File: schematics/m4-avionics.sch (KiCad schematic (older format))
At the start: 3 parts

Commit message: Rename schematics folder and delete old board template
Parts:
- added J?: CAMERA, symbol cusf-kicad:CONN_02x12
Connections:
- net 3v3: now also J?.1, J?.2, J?.3, J?.4
- net GND: now also J?.21, J?.22, J?.23, J?.24
- new net DCMI_D0: J?.5
- new net DCMI_D1: J?.6
- new net DCMI_D2: J?.7
- new net DCMI_D3: J?.8
- new net DCMI_D4: J?.9
- new net DCMI_D5: J?.10
- new net DCMI_D6: J?.11
- new net DCMI_D7: J?.12
- new net DCMI_HSYNC: J?.13
- new net DCMI_NRST: J?.16
- new net DCMI_PIXCLK: J?.17
- new net DCMI_PWR_EN: J?.14
- new net DCMI_SCL: J?.20
- new net DCMI_SDA: J?.18
- new net DCMI_VSYNC: J?.15
- no-connect marks 0 -> 1
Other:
- note added: "CAMERA INTERCONNECT"
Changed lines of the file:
@@
 Text Label 1300 5650 0    50   ~ 0
 CAN_BUS
+$Comp
+L cusf-kicad:CONN_02x12 J?
+U 1 1 621A1F39
+P 9900 3900
+F 0 "J?" H 9850 4000 50  0000 C CNN
+F 1 "CAMERA" H 9850 2700 50  0000 C CNN
+F 2 "" H 9900 3900 50  0001 C CNN
+F 3 "" H 9900 3900 50  0001 C CNN
+	1    9900 3900
+	1    0    0    -1
+$EndComp
+Wire Wire Line
+	9700 4000 9600 4000
+Wire Wire Line
+	9600 4000 9600 3900
+Wire Wire Line
+	9600 3900 9700 3900
+Wire Wire Line
+	10000 3900 10100 3900
+Wire Wire Line
+	10100 3900 10100 4000
+Wire Wire Line
+	10000 4000 10100 4000
+Wire Wire Line
+	10100 3900 10100 3750
+Connection ~ 10100 3900
+Wire Wire Line
+	9600 3750 9600 3900
+Connection ~ 9600 3900
+$Comp
+L cusf-kicad:3v3 #PWR?
+U 1 1 621A1F49
+P 9600 3750
+F 0 "#PWR?" H 9600 3860 50  0001 L CNN
+F 1 "3v3" H 9600 3850 50  0000 C CNN
+F 2 "" H 9600 3750 50  0001 C CNN
+F 3 "" H 9600 3750 50  0001 C CNN
+	1    9600 3750
+	1    0    0    -1
+$EndComp
+$Comp
+L cusf-kicad:3v3 #PWR?
+U 1 1 621A1F4F
+P 10100 3750
+F 0 "#PWR?" H 10100 3860 50  0001 L CNN
+F 1 "3v3" H 10100 3850 50  0000 C CNN
+F 2 "" H 10100 3750 50  0001 C CNN
+F 3 "" H 10100 3750 50  0001 C CNN
+	1    10100 3750
+	1    0    0    -1
+$EndComp
+Wire Wire Line
+	9700 5000 9600 5000
+Wire Wire Line
+	9600 5000 9600 5150
+Wire Wire Line
+	9600 5000 9600 4900
+Wire Wire Line
+	9600 4900 9700 4900
+Connection ~ 9600 5000
+Wire Wire Line
+	10000 5000 10100 5000
+Wire Wire Line
+	10100 5000 10100 5150
+Wire Wire Line
+	10100 5000 10100 4900
+Wire Wire Line
+	10100 4900 10000 4900
+Connection ~ 10100 5000
+$Comp
+L cusf-kicad:GND #PWR?
+U 1 1 621A1F5F
+P 9600 5150
+F 0 "#PWR?" H 9470 5190 50  0001 L CNN
+F 1 "GND" H 9600 5050 50  0000 C CNN
+F 2 "" H 9600 5150 50  0001 C CNN
+F 3 "" H 9600 5150 50  0001 C CNN
+	1    9600 5150
+	1    0    0    -1
+$EndComp
+$Comp
+L cusf-kicad:GND #PWR?
+U 1 1 621A1F65
+P 10100 5150
+F 0 "#PWR?" H 9970 5190 50  0001 L CNN
+F 1 "GND" H 10100 5050 50  0000 C CNN
+F 2 "" H 10100 5150 50  0001 C CNN
+F 3 "" H 10100 5150 50  0001 C CNN
+	1    10100 5150
+	1    0    0    -1
+$EndComp
+Wire Wire Line
+	9700 4100 9600 4100
+Wire Wire Line
+	9700 4200 9600 4200
+Wire Wire Line
+	9700 4300 9600 4300
+Wire Wire Line
+	9700 4400 9600 4400
+Wire Wire Line
+	9700 4500 9600 4500
+Wire Wire Line
+	10000 4100 10100 4100
+Wire Wire Line
+	10000 4200 10100 4200
+Wire Wire Line
+	10000 4300 10100 4300
+Wire Wire Line
+	10000 4400 10100 4400
+Wire Wire Line
+	10000 4500 10100 4500
+Wire Wire Line
+	10100 4600 10000 4600
+Wire Wire Line
+	10100 4700 10000 4700
+Wire Wire Line
+	9600 4700 9700 4700
+Wire Wire Line
+	9600 4600 9700 4600
+Text Label 10100 4100 0    50   ~ 0
+DCMI_D1
+Text Label 10100 4200 0    50   ~ 0
+DCMI_D3
+Text Label 10100 4300 0    50   ~ 0
+DCMI_D5
+Text Label 10100 4400 0    50   ~ 0
+DCMI_D7
+Text Label 9600 4400 2    50   ~ 0
+DCMI_D6
+Text Label 9600 4300 2    50   ~ 0
+DCMI_D4
+Text Label 9600 4200 2    50   ~ 0
+DCMI_D2
+Text Label 9600 4100 2    50   ~ 0
+DCMI_D0
+Text Label 9600 4700 2    50   ~ 0
+DCMI_PIXCLK
+Text Label 9600 4600 2    50   ~ 0
+DCMI_VSYNC
+Text Label 9600 4500 2    50   ~ 0
+DCMI_HSYNC
+Text Label 10100 4500 0    50   ~ 0
+DCMI_PWR_EN
+Text Label 10100 4600 0    50   ~ 0
+DCMI_NRST
+Wire Notes Line
+	8950 3400 10800 3400
+Wire Notes Line
+	10800 3400 10800 5550
+Wire Notes Line
+	10800 5550 8950 5550
+Wire Notes Line
+	8950 3400 8950 5550
+Text Notes 8950 3350 0    98   ~ 20
+CAMERA INTERCONNECT
+Wire Wire Line
+	10000 4800 10100 4800
+Text Label 10100 4700 0    50   ~ 0
+DCMI_SDA
+Text Label 10100 4800 0    50   ~ 0
+DCMI_SCL
+NoConn ~ 9700 4800
+Wire Wire Line
+	2650 1200 2800 1200
+Wire Wire Line
+	2650 2250 2800 2250
+Wire Wire Line
+	2650 3400 2800 3400
+$Comp
+L cusf-kicad:GND #PWR?
+U 1 1 621AB80D
+P 2800 3400
+F 0 "#PWR?" H 2670 3440 50  0001 L CNN
+F 1 "GND" V 2800 3150 50  0000 L CNN
+F 2 "" H 2800 3400 50  0001 C CNN
+F 3 "" H 2800 3400 50  0001 C CNN
+	1    2800 3400
+	0    -1   -1   0
+$EndComp
+$Comp
+L cusf-kicad:GND #PWR?
+U 1 1 621B0D14
+P 2800 2250
+F 0 "#PWR?" H 2670 2290 50  0001 L CNN
+F 1 "GND" V 2800 2000 50  0000 L CNN
+F 2 "" H 2800 2250 50  0001 C CNN
+F 3 "" H 2800 2250 50  0001 C CNN
+	1    2800 2250
+	0    -1   -1   0
+$EndComp
+$Comp
+L cusf-kicad:GND #PWR?
+U 1 1 621B11B9
+P 2800 1200
+F 0 "#PWR?" H 2670 1240 50  0001 L CNN
+F 1 "GND" V 2800 950 50  0000 L CNN
+F 2 "" H 2800 1200 50  0001 C CNN
+F 3 "" H 2800 1200 50  0001 C CNN
+	1    2800 1200
+	0    -1   -1   0
+$EndComp
 Wire Bus Line
 	1200 3800 1200 5500

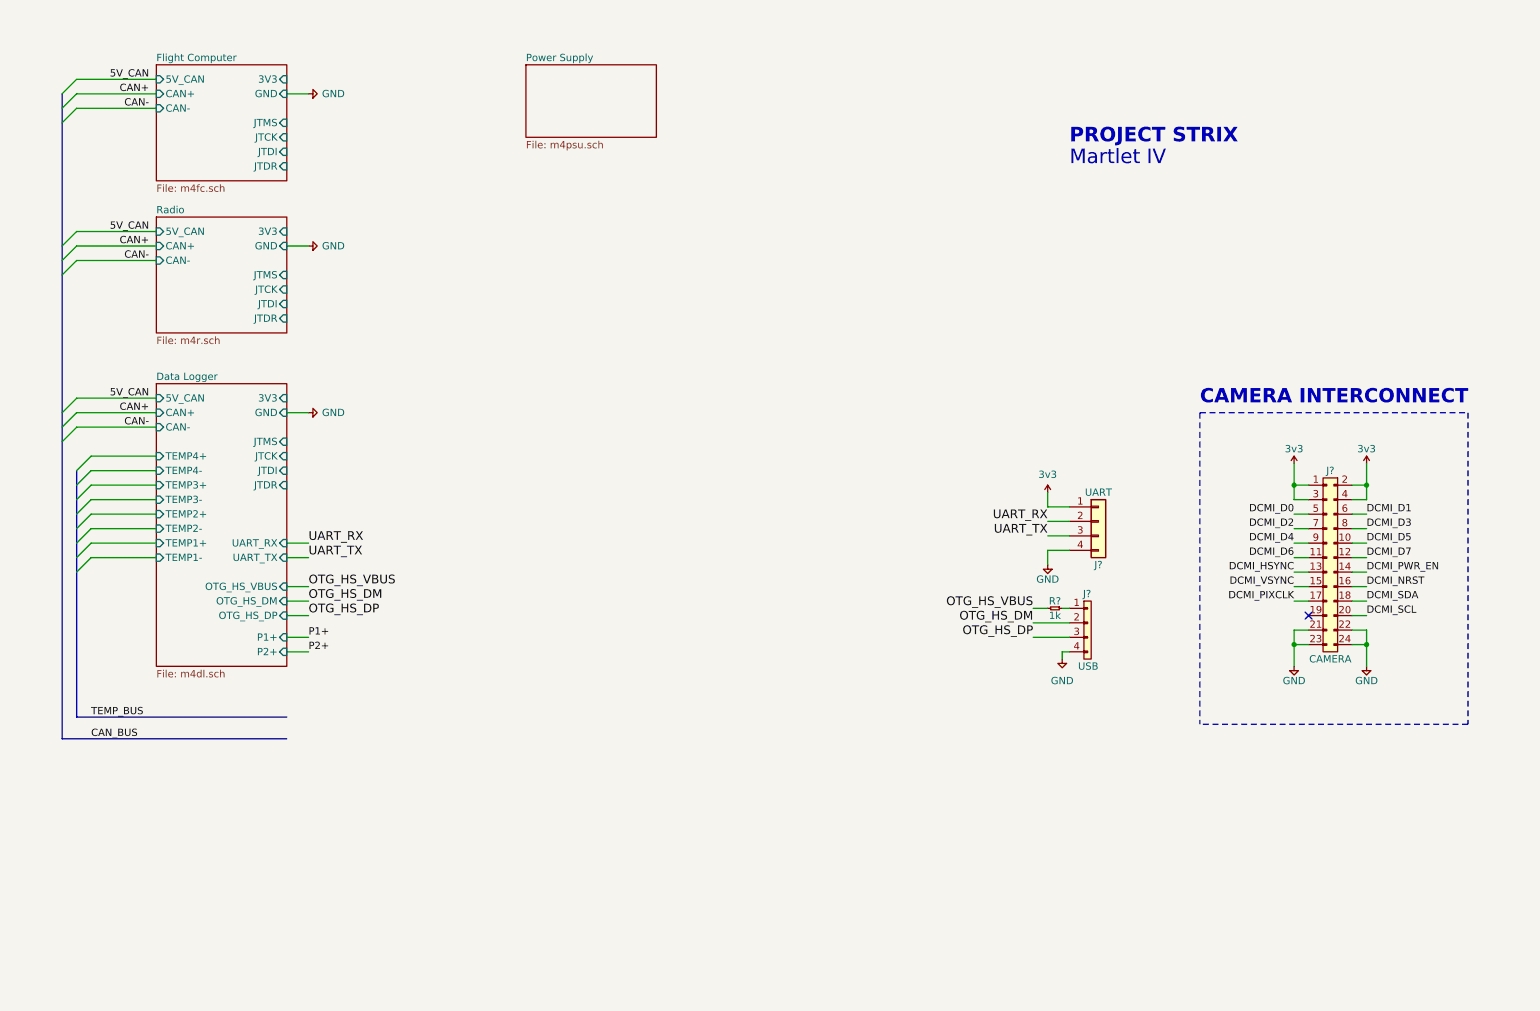
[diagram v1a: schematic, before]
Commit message: Chain JTAG connections
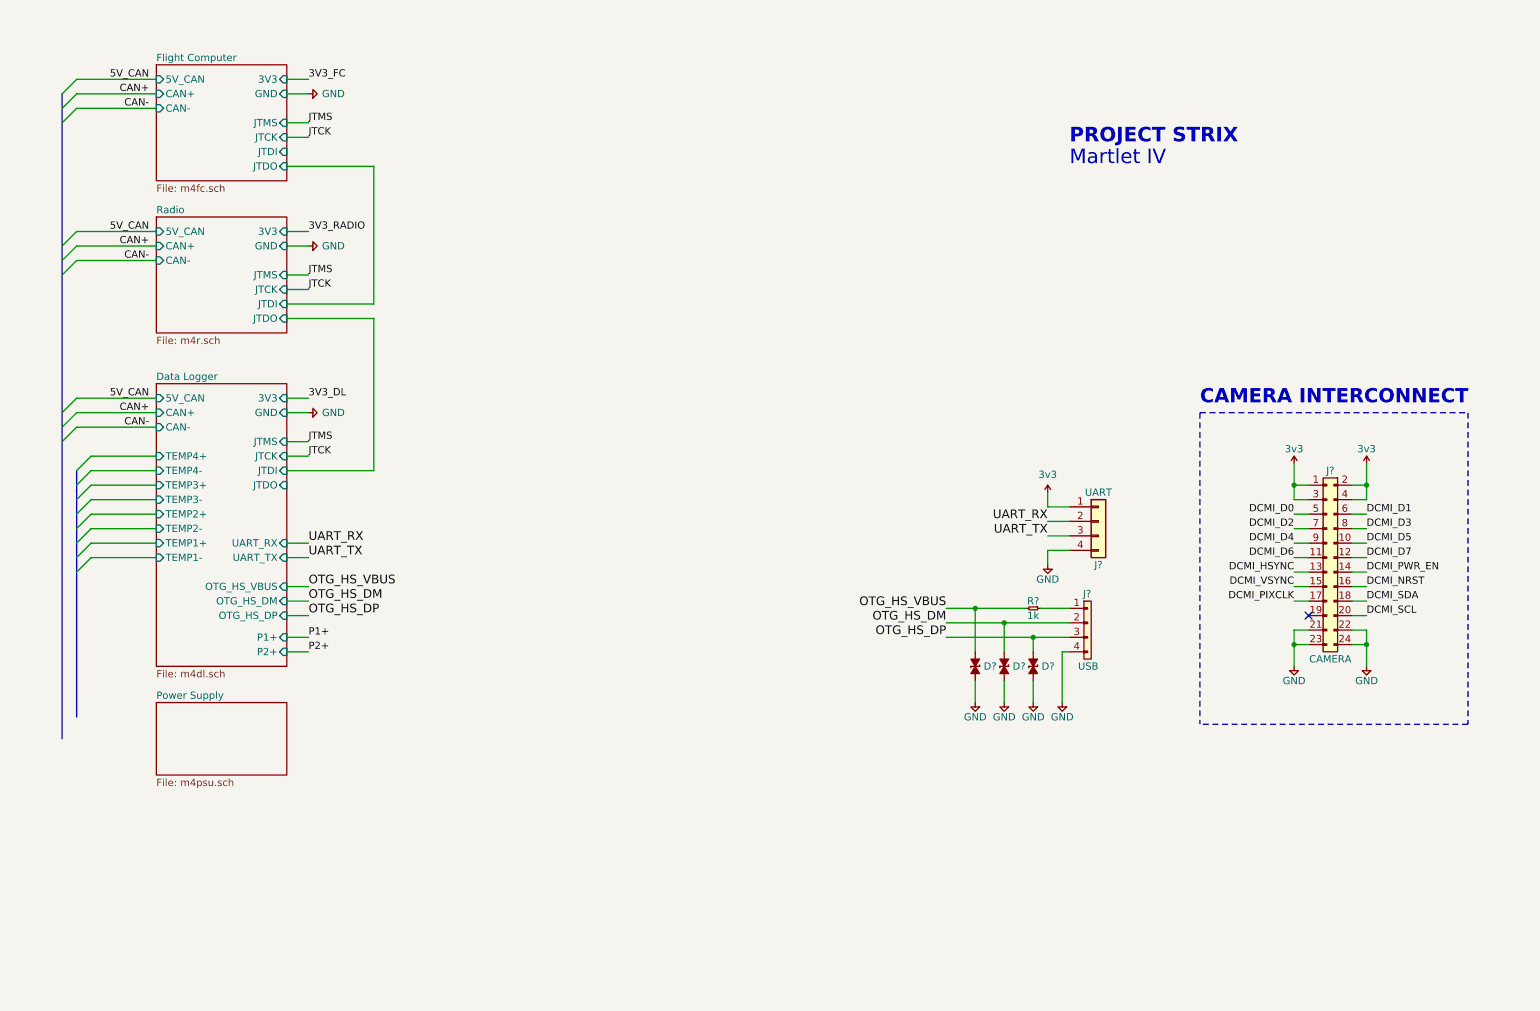
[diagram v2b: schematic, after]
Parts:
- added D? (x3): ESD_DIODE, cusf:0402, symbol cusf-kicad:ESD_DIODE
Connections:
- net GND: now also D?.2, D?.2, D?.2
- net OTG_HS_DM: now also D?.1
- net OTG_HS_DP: now also D?.1
- net OTG_HS_VBUS: now also D?.1
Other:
- moved on the sheet: R?
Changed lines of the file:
@@
 F8 "JTCK" I R 2650 3700 50
 F9 "JTDI" I R 2650 3800 50
-F10 "JTDR" I R 2650 3900 50
-F11 "TEMP4+" I L 1750 3700 50
-F12 "TEMP4-" I L 1750 3800 50
-F13 "TEMP3+" I L 1750 3900 50
-F14 "TEMP3-" I L 1750 4000 50
-F15 "TEMP2+" I L 1750 4100 50
-F16 "TEMP2-" I L 1750 4200 50
-F17 "TEMP1+" I L 1750 4300 50
-F18 "TEMP1-" I L 1750 4400 50
-F19 "3V3" I R 2650 3300 50
-F20 "GND" I R 2650 3400 50
-F21 "OTG_HS_VBUS" I R 2650 4600 50
-F22 "OTG_HS_DM" I R 2650 4700 50
-F23 "OTG_HS_DP" I R 2650 4800 50
-F24 "P1+" I R 2650 4950 50
-F25 "P2+" I R 2650 5050 50
+F10 "TEMP4+" I L 1750 3700 50
+F11 "TEMP4-" I L 1750 3800 50
+F12 "TEMP3+" I L 1750 3900 50
+F13 "TEMP3-" I L 1750 4000 50
+F14 "TEMP2+" I L 1750 4100 50
+F15 "TEMP2-" I L 1750 4200 50
+F16 "TEMP1+" I L 1750 4300 50
+F17 "TEMP1-" I L 1750 4400 50
+F18 "3V3" I R 2650 3300 50
+F19 "GND" I R 2650 3400 50
+F20 "OTG_HS_VBUS" I R 2650 4600 50
+F21 "OTG_HS_DM" I R 2650 4700 50
+F22 "OTG_HS_DP" I R 2650 4800 50
+F23 "P1+" I R 2650 4950 50
+F24 "P2+" I R 2650 5050 50
+F25 "JTDO" I R 2650 3900 50
 $EndSheet
 $Sheet
-S 4300 1000 900  500
+S 1750 5400 900  500
 U 6013B1F2
 F0 "Power Supply" 50
@@
 CAN-
 $Sheet
-S 1750 1000 900  800
-U 6013AEF4
-F0 "Flight Computer" 50
-F1 "m4fc.sch" 50
-F2 "5V_CAN" I L 1750 1100 50
-F3 "CAN+" I L 1750 1200 50
-F4 "CAN-" I L 1750 1300 50
-F5 "JTMS" I R 2650 1400 50
-F6 "JTCK" I R 2650 1500 50
-F7 "JTDI" I R 2650 1600 50
-F8 "JTDR" I R 2650 1700 50
-F9 "3V3" I R 2650 1100 50
-F10 "GND" I R 2650 1200 50
-$EndSheet
-$Sheet
 S 1750 2050 900  800
 U 6013B1C8
@@
 F6 "JTCK" I R 2650 2550 50
 F7 "JTDI" I R 2650 2650 50
-F8 "JTDR" I R 2650 2750 50
-F9 "3V3" I R 2650 2150 50
-F10 "GND" I R 2650 2250 50
+F8 "3V3" I R 2650 2150 50
+F9 "GND" I R 2650 2250 50
+F10 "JTDO" I R 2650 2750 50
 $EndSheet
 $Bitmap
@@
 L cusf-kicad:R R?
 U 1 1 61A0226B
-P 8000 4750
+P 7850 4750
 AR Path="/6013AE2F/61A0226B" Ref="R?"  Part="1"
 AR Path="/61A0226B" Ref="R?"  Part="1"
-F 0 "R?" H 8050 4800 50  0000 C CNN
-F 1 "1k" H 8050 4700 50  0000 C CNN
-F 2 "" H 8000 4750 50  0001 C CNN
-F 3 "" H 8000 4750 50  0001 C CNN
-	1    8000 4750
+F 0 "R?" H 7900 4800 50  0000 C CNN
+F 1 "1k" H 7900 4700 50  0000 C CNN
+F 2 "" H 7850 4750 50  0001 C CNN
+F 3 "" H 7850 4750 50  0001 C CNN
+	1    7850 4750
 	-1   0    0    -1
 $EndComp
@@
 L cusf-kicad:GND #PWR?
 U 1 1 61A02271
-P 8000 5100
+P 8000 5400
 AR Path="/6013AE2F/61A02271" Ref="#PWR?"  Part="1"
 AR Path="/61A02271" Ref="#PWR?"  Part="1"
-F 0 "#PWR?" H 8000 4850 50  0001 C CNN
-F 1 "GND" H 8000 4950 50  0000 C CNN
-F 2 "" H 8000 5100 50  0000 C CNN
-F 3 "" H 8000 5100 50  0000 C CNN
-	1    8000 5100
+F 0 "#PWR?" H 8000 5150 50  0001 C CNN
+F 1 "GND" H 8000 5300 50  0000 C CNN
+F 2 "" H 8000 5400 50  0000 C CNN
+F 3 "" H 8000 5400 50  0000 C CNN
+	1    8000 5400
 	-1   0    0    -1
 $EndComp
-Text Label 7800 4750 2    60   ~ 0
+Text Label 7200 4750 2    60   ~ 0
 OTG_HS_VBUS
-Text Label 7800 4850 2    60   ~ 0
+Text Label 7200 4850 2    60   ~ 0
 OTG_HS_DM
-Text Label 7800 4950 2    60   ~ 0
+Text Label 7200 4950 2    60   ~ 0
 OTG_HS_DP
 $Comp
@@
 $EndComp
 Wire Wire Line
-	8000 5050 8000 5100
-Wire Wire Line
-	8050 4750 8000 4750
+	8000 5050 8000 5400
+Wire Wire Line
+	8050 4750 7850 4750
 Wire Wire Line
 	8050 5050 8000 5050
@@
 	8050 4950 7800 4950
 Wire Wire Line
-	7800 4850 8050 4850
-Wire Wire Line
-	7900 4750 7800 4750
+	7200 4850 7600 4850
+Wire Wire Line
+	7750 4750 7400 4750
 Wire Wire Line
 	8050 4250 7900 4250
@@
 Wire Wire Line
 	2800 4400 2650 4400
-Wire Bus Line
-	1200 5500 2650 5500
 Entry Wire Line
 	1300 4300 1200 4400
@@
 Entry Wire Line
 	1200 1300 1100 1400
-Wire Bus Line
-	1100 5650 2650 5650
-Text Label 1300 5500 0    50   ~ 0
-TEMP_BUS
-Text Label 1300 5650 0    50   ~ 0
-CAN_BUS
 $Comp
 L cusf-kicad:CONN_02x12 J?
@@
 	0    -1   -1   0
 $EndComp
+$Sheet
+S 1750 1000 900  800
+U 6013AEF4
+F0 "Flight Computer" 50
+F1 "m4fc.sch" 50
+F2 "5V_CAN" I L 1750 1100 50
+F3 "CAN+" I L 1750 1200 50
+F4 "CAN-" I L 1750 1300 50
+F5 "JTMS" I R 2650 1400 50
+F6 "JTCK" I R 2650 1500 50
+F7 "JTDI" I R 2650 1600 50
+F8 "3V3" I R 2650 1100 50
+F9 "GND" I R 2650 1200 50
+F10 "JTDO" I R 2650 1700 50
+$EndSheet
+Wire Wire Line
+	2650 1700 3250 1700
+Wire Wire Line
+	3250 1700 3250 2650
+Wire Wire Line
+	3250 2650 2650 2650
+Wire Wire Line
+	2650 2750 3250 2750
+Wire Wire Line
+	3250 2750 3250 3800
+Wire Wire Line
+	3250 3800 2650 3800
+Wire Wire Line
+	2650 1500 2800 1500
+Wire Wire Line
+	2650 1400 2800 1400
+Text Label 2800 1400 0    50   ~ 0
+JTMS
+Text Label 2800 1500 0    50   ~ 0
+JTCK
+Wire Wire Line
+	2650 2550 2800 2550
+Wire Wire Line
+	2650 2450 2800 2450
+Text Label 2800 2450 0    50   ~ 0
+JTMS
+Text Label 2800 2550 0    50   ~ 0
+JTCK
+Wire Wire Line
+	2650 3700 2800 3700
+Wire Wire Line
+	2650 3600 2800 3600
+Text Label 2800 3600 0    50   ~ 0
+JTMS
+Text Label 2800 3700 0    50   ~ 0
+JTCK
+Wire Wire Line
+	2650 3300 2800 3300
+Text Label 2800 3300 0    50   ~ 0
+3V3_DL
+Wire Wire Line
+	2650 2150 2800 2150
+Text Label 2800 2150 0    50   ~ 0
+3V3_RADIO
+Wire Wire Line
+	2650 1100 2800 1100
+Text Label 2800 1100 0    50   ~ 0
+3V3_FC
+$Comp
+L cusf-kicad:ESD_DIODE D?
+U 1 1 601F8D2D
+P 7400 5150
+F 0 "D?" V 7400 5208 50  0000 L CNN
+F 1 "ESD_DIODE" H 7350 5050 50  0001 L CNN
+F 2 "cusf:0402" H 7350 4950 50  0001 L CNN
+F 3 "" H 7300 5150 50  0001 C CNN
+F 4 "2368169" H 7350 4850 50  0001 L CNN "Farnell"
+	1    7400 5150
+	0    1    1    0
+$EndComp
+$Comp
+L cusf-kicad:ESD_DIODE D?
+U 1 1 601F9429
+P 7600 5150
+F 0 "D?" V 7600 5208 50  0000 L CNN
+F 1 "ESD_DIODE" H 7550 5050 50  0001 L CNN
+F 2 "cusf:0402" H 7550 4950 50  0001 L CNN
+F 3 "" H 7500 5150 50  0001 C CNN
+F 4 "2368169" H 7550 4850 50  0001 L CNN "Farnell"
+	1    7600 5150
+	0    1    1    0
+$EndComp
+$Comp
+L cusf-kicad:ESD_DIODE D?
+U 1 1 601F98EE
+P 7800 5150
+F 0 "D?" V 7800 5208 50  0000 L CNN
+F 1 "ESD_DIODE" H 7750 5050 50  0001 L CNN
+F 2 "cusf:0402" H 7750 4950 50  0001 L CNN
+F 3 "" H 7700 5150 50  0001 C CNN
+F 4 "2368169" H 7750 4850 50  0001 L CNN "Farnell"
+	1    7800 5150
+	0    1    1    0
+$EndComp
+Wire Wire Line
+	7800 5050 7800 4950
+Connection ~ 7800 4950
+Wire Wire Line
+	7800 4950 7200 4950
+Wire Wire Line
+	7600 5050 7600 4850
+Connection ~ 7600 4850
+Wire Wire Line
+	7600 4850 8050 4850
+Wire Wire Line
+	7400 5050 7400 4750
+Connection ~ 7400 4750
+Wire Wire Line
+	7400 4750 7200 4750
+Wire Wire Line
+	7800 5250 7800 5400
+Wire Wire Line
+	7600 5250 7600 5400
+Wire Wire Line
+	7400 5250 7400 5400
+$Comp
+L cusf-kicad:GND #PWR?
+U 1 1 60221ACF
+P 7800 5400
+AR Path="/6013AE2F/60221ACF" Ref="#PWR?"  Part="1"
+AR Path="/60221ACF" Ref="#PWR?"  Part="1"
+F 0 "#PWR?" H 7800 5150 50  0001 C CNN
+F 1 "GND" H 7800 5300 50  0000 C CNN
+F 2 "" H 7800 5400 50  0000 C CNN
+F 3 "" H 7800 5400 50  0000 C CNN
+	1    7800 5400
+	-1   0    0    -1
+$EndComp
+$Comp
+L cusf-kicad:GND #PWR?
+U 1 1 60221D88
+P 7600 5400
+AR Path="/6013AE2F/60221D88" Ref="#PWR?"  Part="1"
+AR Path="/60221D88" Ref="#PWR?"  Part="1"
+F 0 "#PWR?" H 7600 5150 50  0001 C CNN
+F 1 "GND" H 7600 5300 50  0000 C CNN
+F 2 "" H 7600 5400 50  0000 C CNN
+F 3 "" H 7600 5400 50  0000 C CNN
+	1    7600 5400
+	-1   0    0    -1
+$EndComp
+$Comp
+L cusf-kicad:GND #PWR?
+U 1 1 60221F09
+P 7400 5400
+AR Path="/6013AE2F/60221F09" Ref="#PWR?"  Part="1"
+AR Path="/60221F09" Ref="#PWR?"  Part="1"
+F 0 "#PWR?" H 7400 5150 50  0001 C CNN
+F 1 "GND" H 7400 5300 50  0000 C CNN
+F 2 "" H 7400 5400 50  0000 C CNN
+F 3 "" H 7400 5400 50  0000 C CNN
+	1    7400 5400
+	-1   0    0    -1
+$EndComp
 Wire Bus Line
